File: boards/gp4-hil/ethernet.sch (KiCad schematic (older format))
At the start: 0 parts

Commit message: Continued HiL test board
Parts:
- added J?: BEL_FUSE_0826-1G1T-23-F, symbol BEL_FUSE_0826-1G1T-23-F
- added U?: KSZ9031RN, symbol KSZ9031RN
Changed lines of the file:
@@
 LIBS:special-azonenberg
 LIBS:xilinx-azonenberg
+LIBS:conn
+LIBS:gp4-hil-cache
 EELAYER 25 0
 EELAYER END
 $Descr A4 11693 8268
 encoding utf-8
-Sheet 1 6
+Sheet 3 7
 Title "GreenPak Hardware-In-Loop Test Platform"
 Date "2016-05-09"
@@
 Comment4 ""
 $EndDescr
+$Comp
+L KSZ9031RN U?
+U 1 1 57316FC3
+P 5200 5150
+F 0 "U?" H 6025 8487 60  0000 C CNN
+F 1 "KSZ9031RN" H 6025 8381 60  0000 C CNN
+F 2 "" H 5200 5150 60  0000 C CNN
+F 3 "" H 5200 5150 60  0000 C CNN
+	1    5200 5150
+	1    0    0    -1
+$EndComp
+$Comp
+L BEL_FUSE_0826-1G1T-23-F J?
+U 1 1 57317077
+P 1600 5250
+F 0 "J?" H 1950 5050 60  0000 L CNN
+F 1 "BEL_FUSE_0826-1G1T-23-F" H 750 4950 60  0000 L CNN
+F 2 "" H 1600 5250 60  0000 C CNN
+F 3 "" H 1600 5250 60  0000 C CNN
+	1    1600 5250
+	-1   0    0    -1
+$EndComp
 $EndSCHEMATC

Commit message: Continued work on gp4-hil board schematic
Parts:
- gave numbers to parts that had none: 2
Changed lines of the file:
@@
 Sheet 3 7
 Title "GreenPak Hardware-In-Loop Test Platform"
-Date "2016-05-09"
+Date "2016-05-10"
 Rev "0.1"
 Comp "Andrew Zonenberg"
@@
 $EndDescr
 $Comp
-L KSZ9031RN U?
+L KSZ9031RN U5
 U 1 1 57316FC3
 P 5200 5150
-F 0 "U?" H 6025 8487 60  0000 C CNN
+F 0 "U5" H 6025 8487 60  0000 C CNN
 F 1 "KSZ9031RN" H 6025 8381 60  0000 C CNN
 F 2 "" H 5200 5150 60  0000 C CNN
@@
 $EndComp
 $Comp
-L BEL_FUSE_0826-1G1T-23-F J?
+L BEL_FUSE_0826-1G1T-23-F J1
 U 1 1 57317077
 P 1600 5250
-F 0 "J?" H 1950 5050 60  0000 L CNN
+F 0 "J1" H 1950 5050 60  0000 L CNN
 F 1 "BEL_FUSE_0826-1G1T-23-F" H 750 4950 60  0000 L CNN
 F 2 "" H 1600 5250 60  0000 C CNN

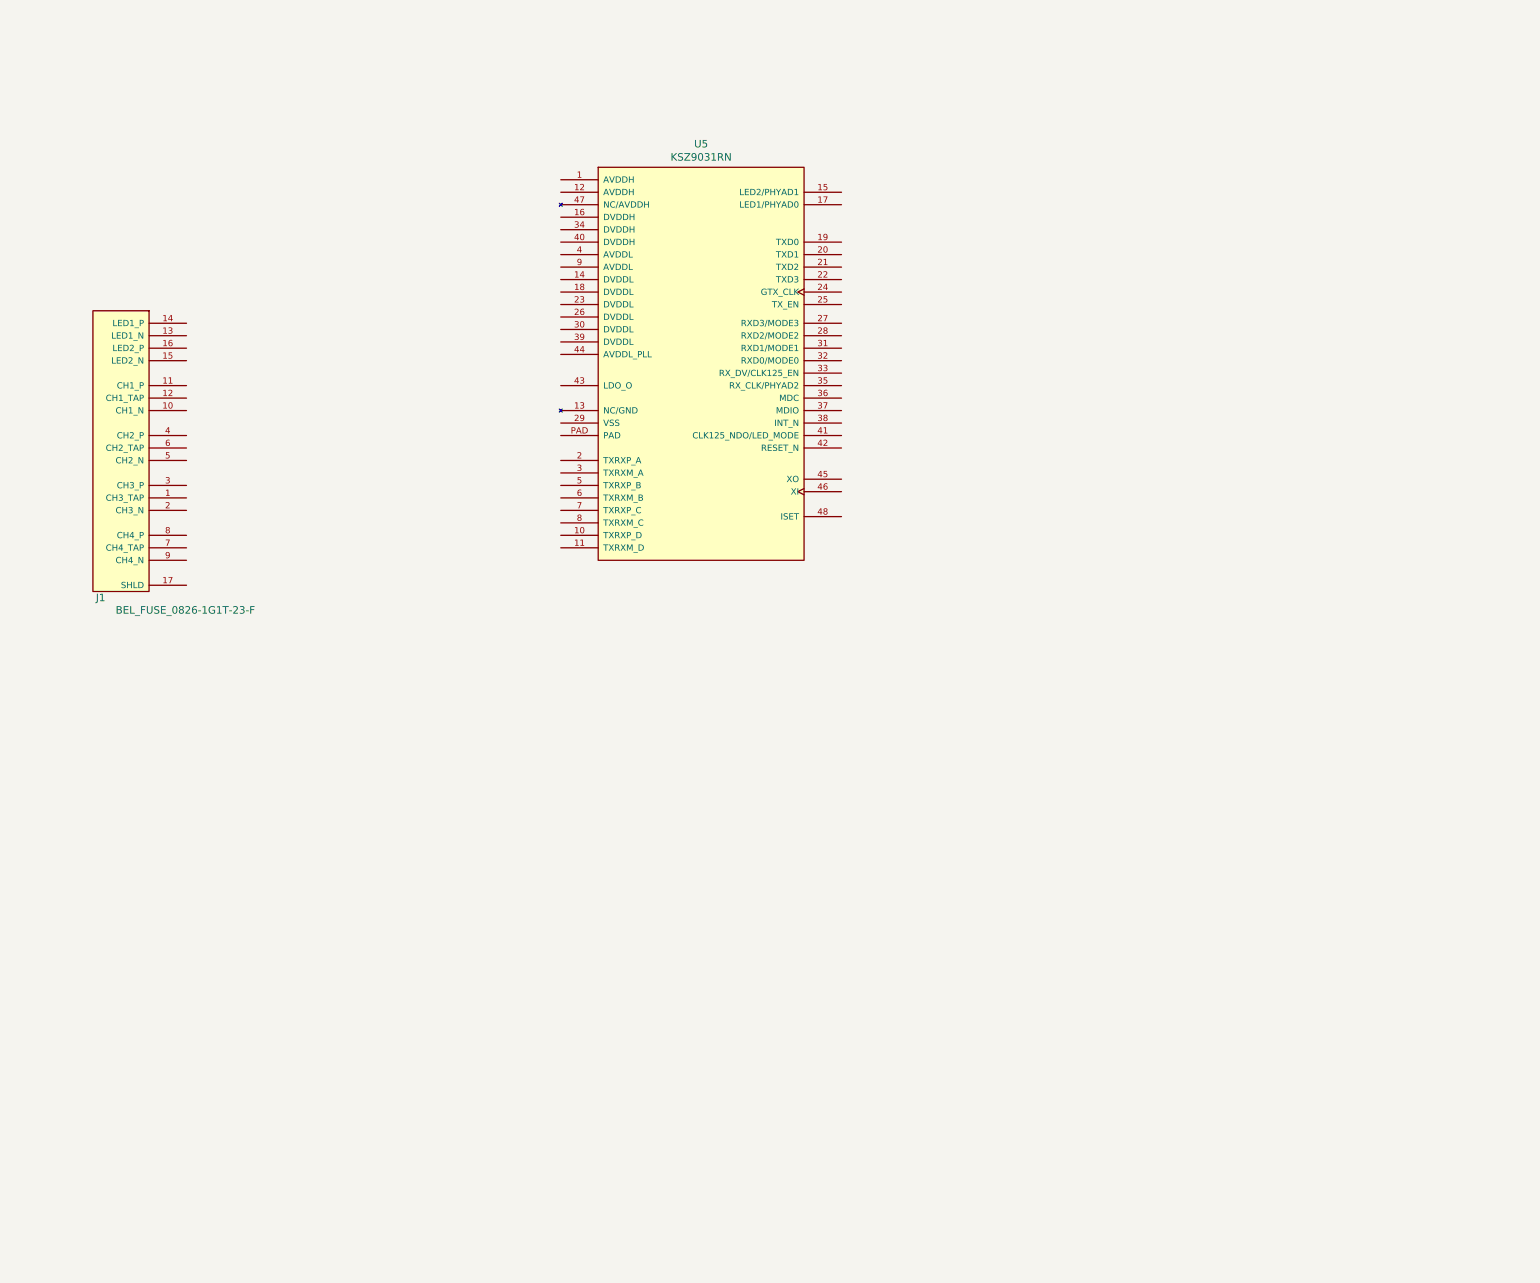
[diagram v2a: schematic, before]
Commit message: Began schematic capture for Ethernet on test board
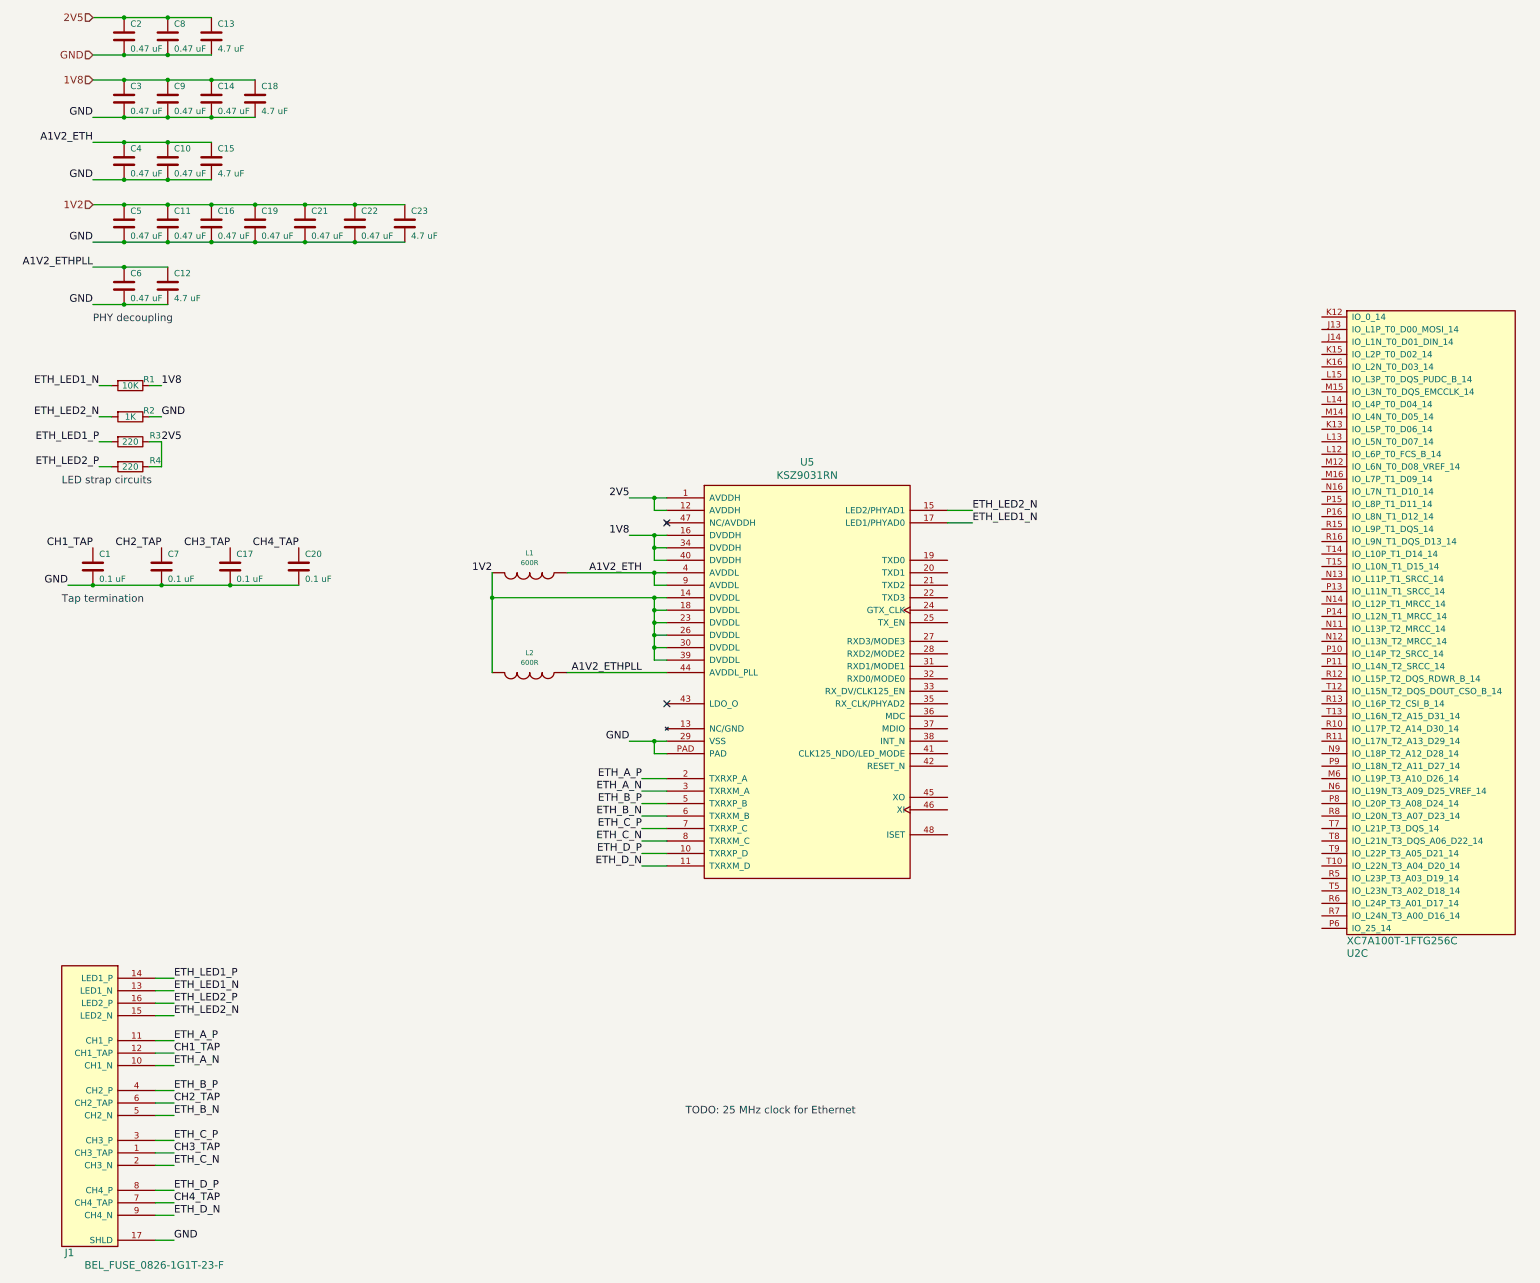
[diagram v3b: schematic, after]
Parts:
- added C1, C17, C20, C7: 0.1 uF, symbol C
- added C10, C11, C14, C16, C19, C2, C21, C22, C3, C4, C5, C6, C8, C9: 0.47 uF, symbol C
- added C12, C13, C15, C18, C23: 4.7 uF, symbol C
- added L1, L2: 600R, symbol INDUCTOR_PWROUT
- added R1: 10K, symbol R
- added R2: 1K, symbol R
- added R3, R4: 220, symbol R
- added U2: XC7A100T-1FTG256C, symbol XC7AxT-xFTG256x
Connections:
- net 2V5: now reaches U5.1 (AVDDH)
- net 2V5: now also U5.12 (AVDDH), C13.1, C2.1, C8.1, R3.1, R4.1
- net ETH_D_P: now reaches U5.10 (TXRXP_D)
- net ETH_D_P: now also J1.8 (CH4_P)
- net ETH_D_N: now reaches U5.11 (TXRXM_D)
- net ETH_D_N: now also J1.9 (CH4_N)
- net 1V2: now reaches U5.14 (DVDDL)
- net 1V2: now also U5.18 (DVDDL), U5.23 (DVDDL), U5.26 (DVDDL), U5.30 (DVDDL), U5.39 (DVDDL), C11.1, C16.1, C19.1, C21.1, C22.1, C23.1, C5.1, L1.2, L2.2
- net ETH_LED2_N: now reaches U5.15 (LED2/PHYAD1)
- net ETH_LED2_N: now also J1.15 (LED2_N), R2.2
- net 1V8: now reaches U5.16 (DVDDH)
- net 1V8: now also U5.34 (DVDDH), U5.40 (DVDDH), C14.1, C18.1, C3.1, C9.1, R1.1
- net ETH_LED1_N: now reaches U5.17 (LED1/PHYAD0)
- net ETH_LED1_N: now also J1.13 (LED1_N), R1.2
- net ETH_A_P: now reaches U5.2 (TXRXP_A)
- net ETH_A_P: now also J1.11 (CH1_P)
- net GND: now reaches U5.29 (VSS)
- net GND: now also J1.17 (SHLD), U5.PAD, C1.2, C10.2, C11.2, C12.2, C13.2, C14.2, C15.2, C16.2, C17.2, C18.2, C19.2, C2.2, C20.2, C21.2, C22.2, C23.2, C3.2, C4.2, C5.2, C6.2, C7.2, C8.2, C9.2, R2.1
- net ETH_A_N: now reaches U5.3 (TXRXM_A)
- net ETH_A_N: now also J1.10 (CH1_N)
- net A1V2_ETH: now reaches U5.4 (AVDDL)
- net A1V2_ETH: now also U5.9 (AVDDL), C10.1, C15.1, C4.1, L1.1
- net A1V2_ETHPLL: now reaches U5.44 (AVDDL_PLL)
- net A1V2_ETHPLL: now also C12.1, C6.1, L2.1
- net ETH_B_P: now reaches U5.5 (TXRXP_B)
- net ETH_B_P: now also J1.4 (CH2_P)
- net ETH_B_N: now reaches U5.6 (TXRXM_B)
- net ETH_B_N: now also J1.5 (CH2_N)
- net ETH_C_P: now reaches U5.7 (TXRXP_C)
- net ETH_C_P: now also J1.3 (CH3_P)
- net ETH_C_N: now reaches U5.8 (TXRXM_C)
- net ETH_C_N: now also J1.2 (CH3_N)
- net CH3_TAP: now reaches J1.1 (CH3_TAP)
- net CH3_TAP: now also C17.1
- net CH1_TAP: now reaches J1.12 (CH1_TAP)
- net CH1_TAP: now also C1.1
- net ETH_LED1_P: now reaches J1.14 (LED1_P)
- net ETH_LED1_P: now also R3.2
- net ETH_LED2_P: now reaches J1.16 (LED2_P)
- net ETH_LED2_P: now also R4.2
- net CH2_TAP: now reaches J1.6 (CH2_TAP)
- net CH2_TAP: now also C7.1
- net CH4_TAP: now reaches J1.7 (CH4_TAP)
- net CH4_TAP: now also C20.1
- no-connect marks 0 -> 2
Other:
- note added: "LED strap circuits"
- note added: "PHY decoupling"
- note added: "TODO: 25 MHz clock for Ethernet"
- note added: "Tap termination"
- moved on the sheet: J1, U5
